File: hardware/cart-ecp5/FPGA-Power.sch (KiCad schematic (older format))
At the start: 2 parts

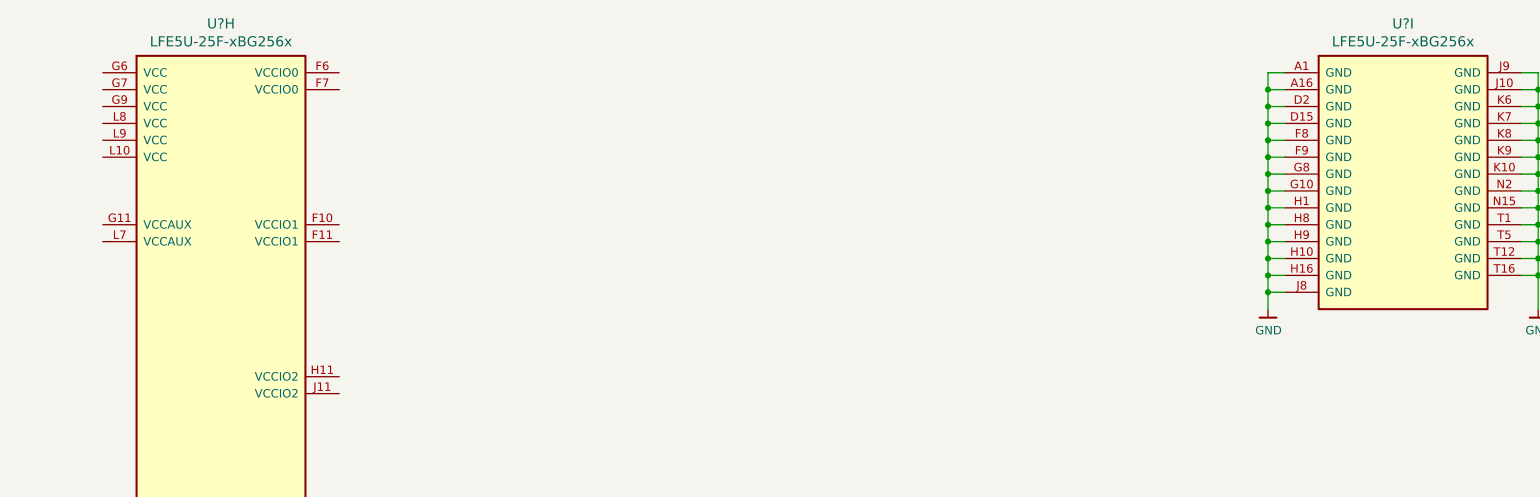
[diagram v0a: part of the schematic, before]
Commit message: First pass annotation and footprint assignment complete
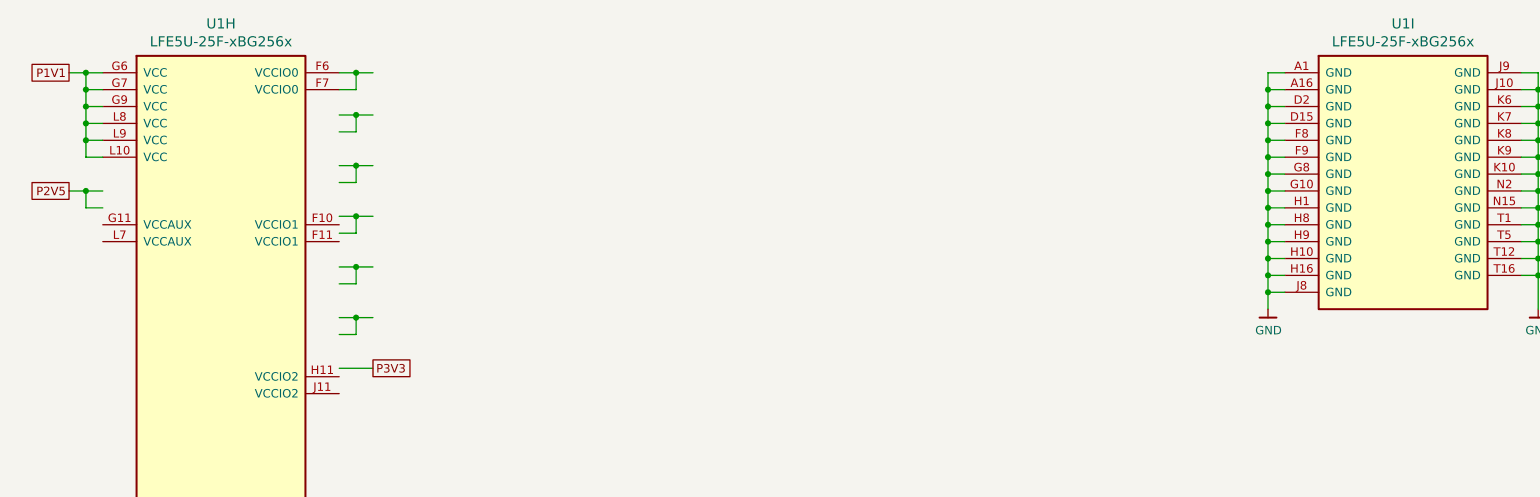
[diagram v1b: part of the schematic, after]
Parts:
- gave numbers to parts that had none: 1
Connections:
- net labels added: P1V1, P2V5, P3V3
- wire segments 54 -> 95
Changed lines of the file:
@@
 $EndDescr
 $Comp
-L ng_fpga_lattice_ecp5:LFE5U-25F-xBG256x U?
+L ng_fpga_lattice_ecp5:LFE5U-25F-xBG256x U1
 U 8 1 5F5F3F21
 P 5000 5000
-F 0 "U?" H 5500 5190 60  0000 C CNN
+F 0 "U1" H 5500 5190 60  0000 C CNN
 F 1 "LFE5U-25F-xBG256x" H 5500 5084 60  0000 C CNN
 F 2 "ng_fpga_lattice_ecp5:LFE5U-25F_BGA-256_14.0x14.0mm_Layout16x16_P0.8mm_Pad0.35mm" H 5750 950 60  0001 C CNN
@@
 $EndComp
 $Comp
-L ng_fpga_lattice_ecp5:LFE5U-25F-xBG256x U?
+L ng_fpga_lattice_ecp5:LFE5U-25F-xBG256x U1
 U 9 1 5F5F3F28
 P 12000 5000
-F 0 "U?" H 12500 5190 60  0000 C CNN
+F 0 "U1" H 12500 5190 60  0000 C CNN
 F 1 "LFE5U-25F-xBG256x" H 12500 5084 60  0000 C CNN
 F 2 "ng_fpga_lattice_ecp5:LFE5U-25F_BGA-256_14.0x14.0mm_Layout16x16_P0.8mm_Pad0.35mm" H 12750 950 60  0001 C CNN
@@
 	11700 6400 11700 6500
 $Comp
-L ng_power:GND #PWR?
+L ng_power:GND #PWR01
 U 1 1 5F5F3F7D
 P 11700 6500
-F 0 "#PWR?" H 11700 6250 50  0001 C CNN
+F 0 "#PWR01" H 11700 6250 50  0001 C CNN
 F 1 "GND" H 11703 6374 50  0000 C CNN
 F 2 "" H 11600 6150 50  0001 C CNN
@@
 $EndComp
 $Comp
-L ng_power:GND #PWR?
+L ng_power:GND #PWR02
 U 1 1 5F5F3F83
 P 13300 6500
-F 0 "#PWR?" H 13300 6250 50  0001 C CNN
+F 0 "#PWR02" H 13300 6250 50  0001 C CNN
 F 1 "GND" H 13303 6374 50  0000 C CNN
 F 2 "" H 13200 6150 50  0001 C CNN
@@
 	1    0    0    -1
 $EndComp
+Wire Wire Line
+	4800 5900 4700 5900
+Wire Wire Line
+	4700 5900 4700 5800
+Wire Wire Line
+	4700 5800 4800 5800
+Wire Wire Line
+	4700 5800 4600 5800
+Connection ~ 4700 5800
+Wire Wire Line
+	4800 5600 4700 5600
+Wire Wire Line
+	4700 5600 4700 5500
+Wire Wire Line
+	4700 5100 4800 5100
+Wire Wire Line
+	4800 5500 4700 5500
+Connection ~ 4700 5500
+Wire Wire Line
+	4700 5500 4700 5400
+Wire Wire Line
+	4700 5400 4800 5400
+Connection ~ 4700 5400
+Wire Wire Line
+	4700 5400 4700 5300
+Wire Wire Line
+	4800 5300 4700 5300
+Connection ~ 4700 5300
+Wire Wire Line
+	4700 5300 4700 5200
+Wire Wire Line
+	4700 5200 4800 5200
+Connection ~ 4700 5200
+Wire Wire Line
+	4700 5200 4700 5100
+Wire Wire Line
+	4700 5100 4600 5100
+Connection ~ 4700 5100
+Text GLabel 4600 5100 0    50   UnSpc ~ 0
+P1V1
+Text GLabel 4600 5800 0    50   UnSpc ~ 0
+P2V5
+Wire Wire Line
+	6200 6850 6400 6850
+Wire Wire Line
+	6200 6650 6300 6650
+Wire Wire Line
+	6300 6650 6300 6550
+Wire Wire Line
+	6300 6550 6200 6550
+Wire Wire Line
+	6200 6250 6300 6250
+Wire Wire Line
+	6300 6250 6300 6350
+Wire Wire Line
+	6300 6350 6200 6350
+Wire Wire Line
+	6200 5950 6300 5950
+Wire Wire Line
+	6300 5950 6300 6050
+Wire Wire Line
+	6300 6050 6200 6050
+Wire Wire Line
+	6200 5650 6300 5650
+Wire Wire Line
+	6200 5750 6300 5750
+Wire Wire Line
+	6300 5750 6300 5650
+Wire Wire Line
+	6200 5350 6300 5350
+Wire Wire Line
+	6300 5350 6300 5450
+Wire Wire Line
+	6300 5450 6200 5450
+Wire Wire Line
+	6200 5100 6300 5100
+Wire Wire Line
+	6300 5100 6300 5200
+Wire Wire Line
+	6300 5200 6200 5200
+Wire Wire Line
+	6300 5100 6400 5100
+Connection ~ 6300 5100
+Wire Wire Line
+	6300 5350 6400 5350
+Connection ~ 6300 5350
+Wire Wire Line
+	6300 5650 6400 5650
+Connection ~ 6300 5650
+Wire Wire Line
+	6300 5950 6400 5950
+Connection ~ 6300 5950
+Wire Wire Line
+	6300 6250 6400 6250
+Connection ~ 6300 6250
+Wire Wire Line
+	6300 6550 6400 6550
+Connection ~ 6300 6550
+Text GLabel 6400 6850 2    50   UnSpc ~ 0
+P3V3
 $EndSCHEMATC

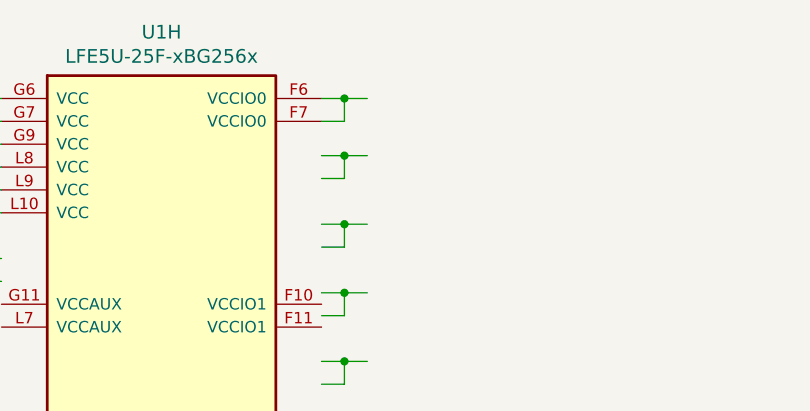
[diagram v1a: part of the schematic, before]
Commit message: Assign FPGA pins for N64 cartridge bus
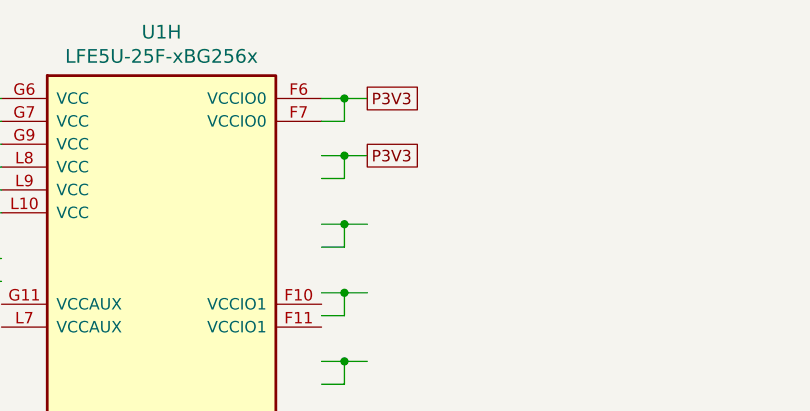
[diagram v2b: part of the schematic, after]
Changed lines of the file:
@@
 Text GLabel 6400 6850 2    50   UnSpc ~ 0
 P3V3
+Text GLabel 6400 5100 2    50   UnSpc ~ 0
+P3V3
+Text GLabel 6400 5350 2    50   UnSpc ~ 0
+P3V3
 $EndSCHEMATC

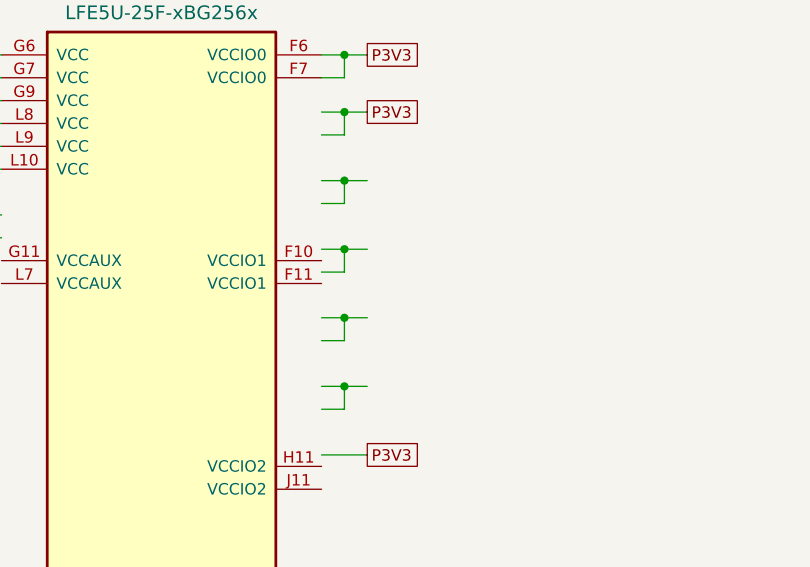
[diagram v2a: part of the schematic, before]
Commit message: Refine placement to make room for power management
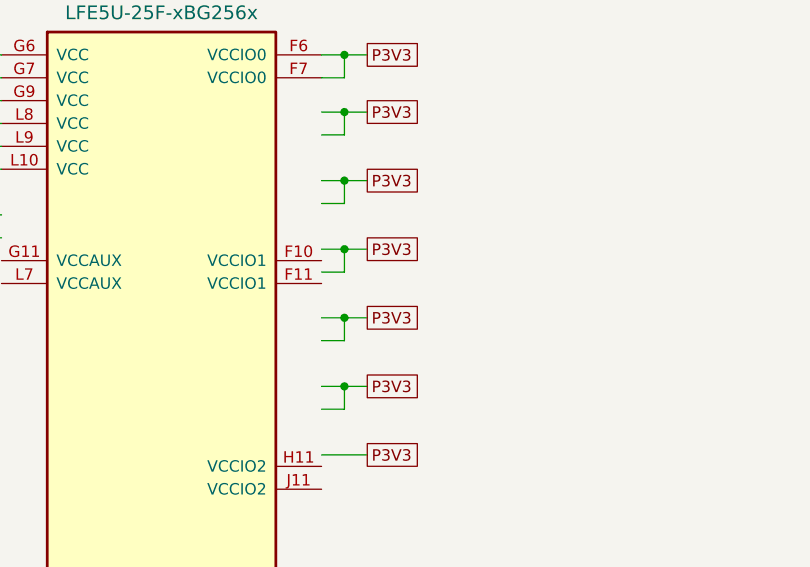
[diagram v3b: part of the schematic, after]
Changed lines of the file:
@@
 Text GLabel 6400 5350 2    50   UnSpc ~ 0
 P3V3
+Text GLabel 6400 5650 2    50   UnSpc ~ 0
+P3V3
+Text GLabel 6400 5950 2    50   UnSpc ~ 0
+P3V3
+Text GLabel 6400 6250 2    50   UnSpc ~ 0
+P3V3
+Text GLabel 6400 6550 2    50   UnSpc ~ 0
+P3V3
 $EndSCHEMATC

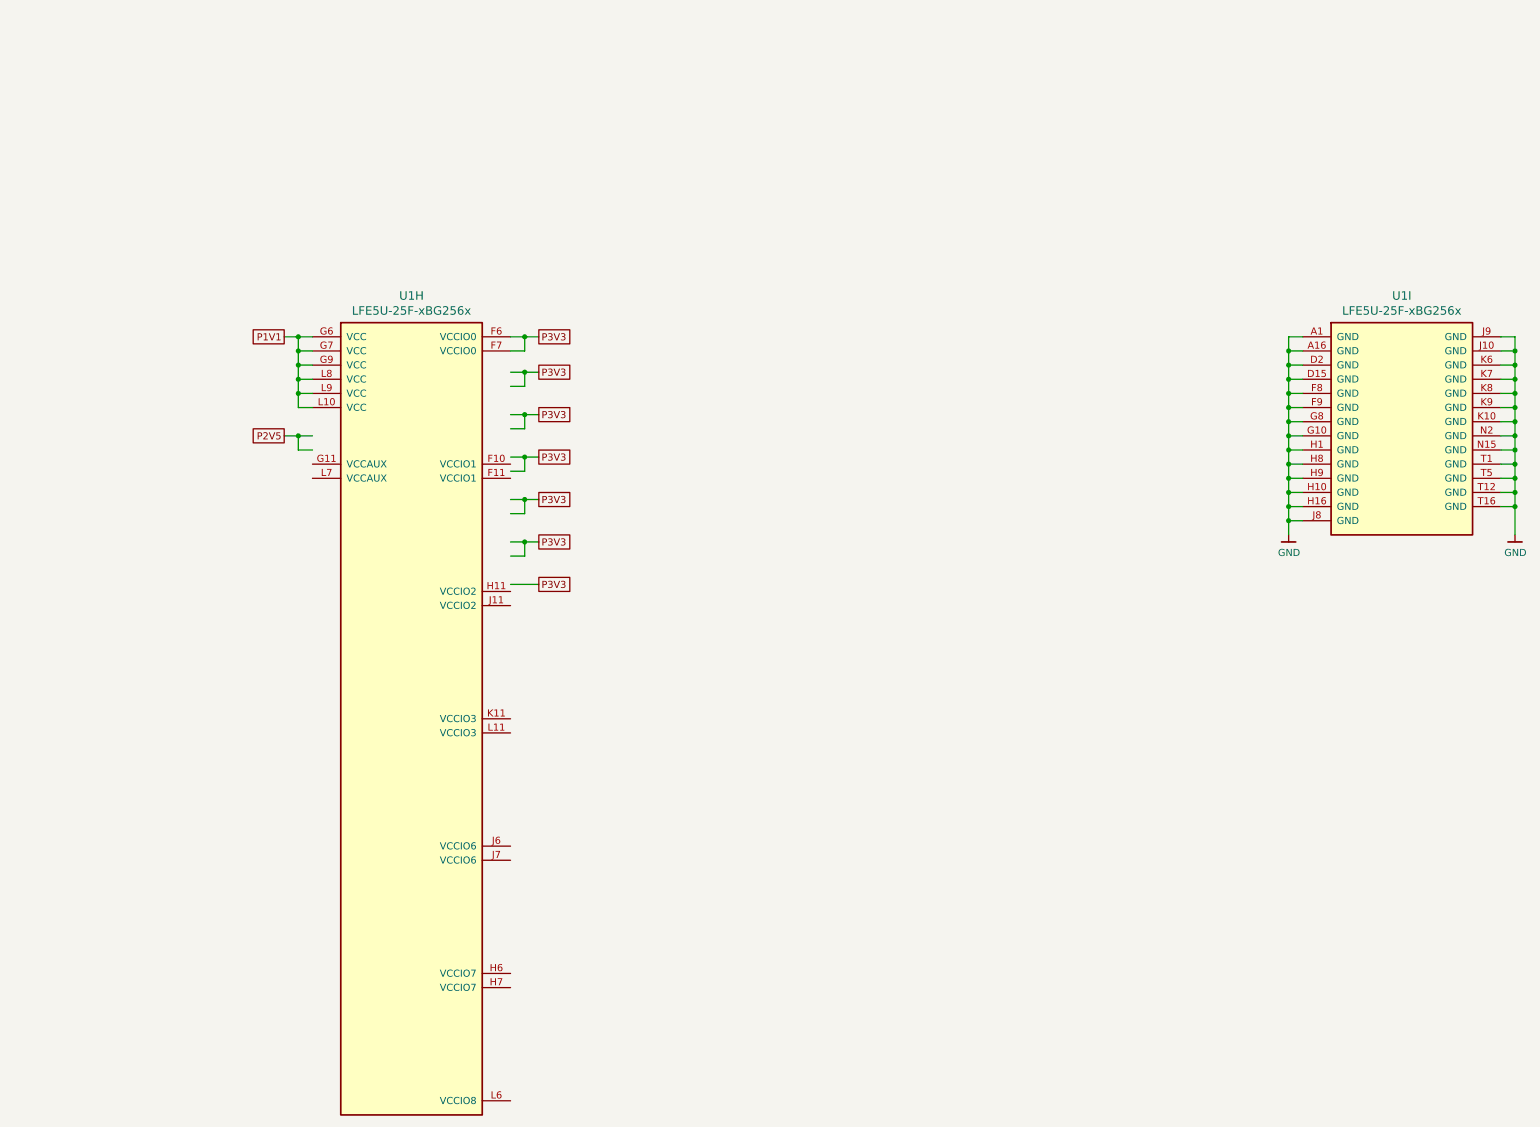
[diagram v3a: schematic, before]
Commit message: Add FPGA decoupling to schematic
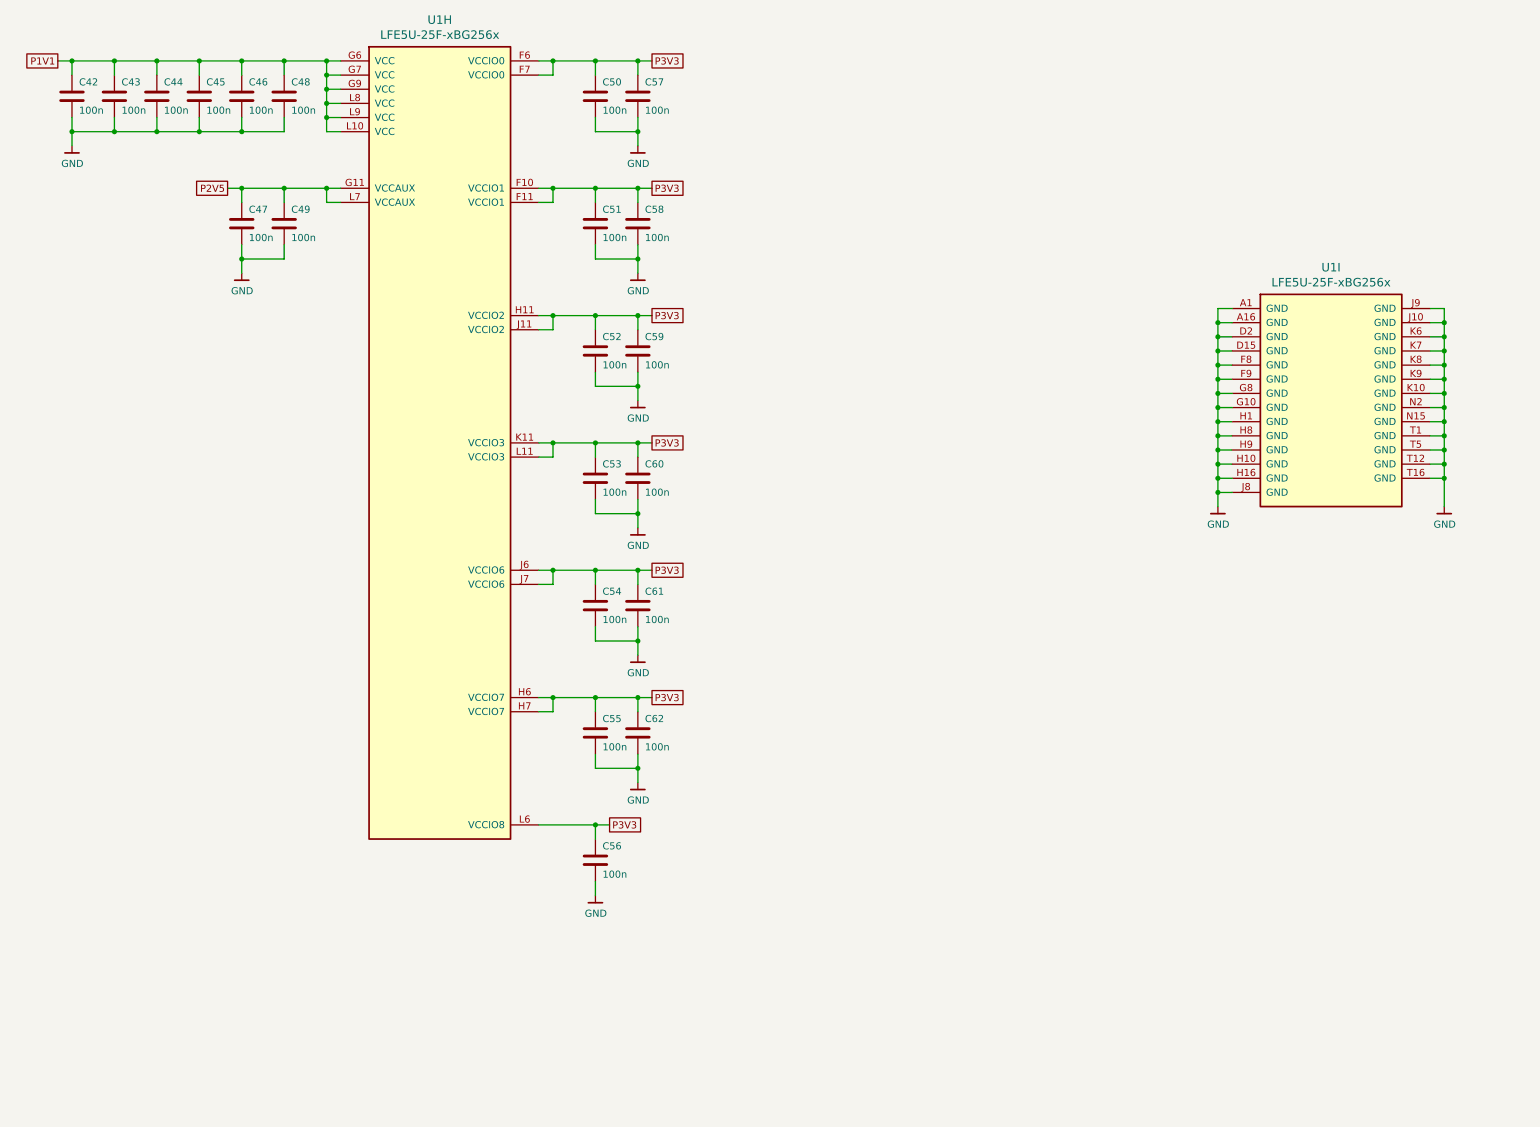
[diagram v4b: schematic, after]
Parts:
- added C42, C43, C44, C45, C46, C47, C48, C49, C50, C51, C52, C53, C54, C55, C56, C57, C58, C59, C60, C61, C62: 100n, Capacitor_SMD:C_0402_1005Metric, symbol Device:C
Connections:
- wire segments 95 -> 178
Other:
- moved on the sheet: U1H, U1I

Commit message: Use 1V8 for HyperRAM interface
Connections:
- net P3V3: no longer C55.1, C62.1, U1.H6 (VCCIO7), U1.H7 (VCCIO7)
- new net P1V8: C55.1, C62.1, U1.H6 (VCCIO7), U1.H7 (VCCIO7)
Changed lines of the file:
@@
 Connection ~ 6500 7650
 Text GLabel 7200 7650 2    50   UnSpc ~ 0
-P3V3
+P1V8
 $Comp
 L Device:C C62

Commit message: Move low-value FPGA decoupling caps to bottom layer
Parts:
- removed C48, C56, C60: 100n, Capacitor_SMD:C_0402_1005Metric, symbol Device:C
- C43, C46, C53, C54, C57, C62: value 100n -> 10n
- C45: value 100n -> 1u
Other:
- moved on the sheet: C42, C43, C44, C45, C46, C50, C51, C52, C53, C54, C57, C58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

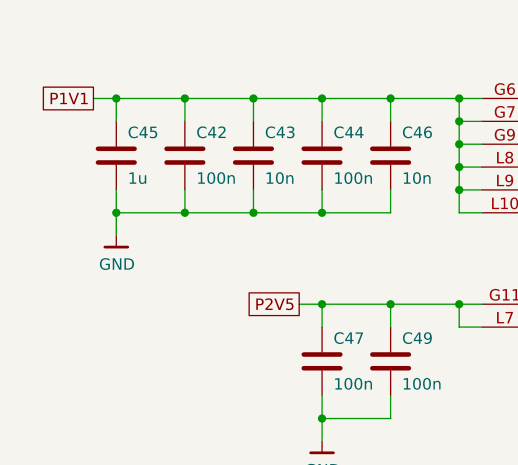
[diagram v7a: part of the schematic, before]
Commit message: Assign FPGA IO for main clock, adjust placement of core switcher
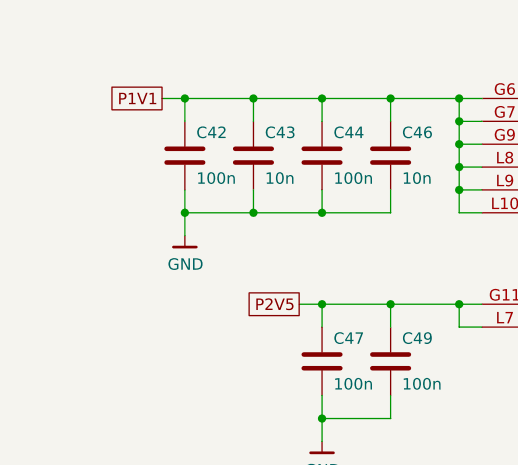
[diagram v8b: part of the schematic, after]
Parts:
- removed C45: 1u, Capacitor_SMD:C_0402_1005Metric, symbol Device:C
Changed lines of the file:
@@
 	4900 3150 4600 3150
 Connection ~ 4900 3150
-Text GLabel 3300 3150 0    50   UnSpc ~ 0
+Text GLabel 3600 3150 0    50   UnSpc ~ 0
 P1V1
 Text GLabel 4200 4050 0    50   UnSpc ~ 0
@@
 L ng_power:GND #PWR01
 U 1 1 5F9193F8
-P 3400 3750
-F 0 "#PWR01" H 3400 3500 50  0001 C CNN
-F 1 "GND" H 3403 3624 50  0000 C CNN
-F 2 "" H 3300 3400 50  0001 C CNN
-F 3 "" H 3400 3750 50  0001 C CNN
-	1    3400 3750
+P 3700 3750
+F 0 "#PWR01" H 3700 3500 50  0001 C CNN
+F 1 "GND" H 3703 3624 50  0000 C CNN
+F 2 "" H 3600 3400 50  0001 C CNN
+F 3 "" H 3700 3750 50  0001 C CNN
+	1    3700 3750
 	1    0    0    -1
 $EndComp
@@
 Wire Wire Line
 	4300 3150 4600 3150
-$Comp
-L Device:C C45
-U 1 1 5F933EBA
-P 3400 3400
-F 0 "C45" H 3450 3500 50  0000 L CNN
-F 1 "1u" H 3450 3300 50  0000 L CNN
-F 2 "Capacitor_SMD:C_0402_1005Metric" H 3438 3250 50  0001 C CNN
-F 3 "~" H 3400 3400 50  0001 C CNN
-	1    3400 3400
-	1    0    0    -1
-$EndComp
 Wire Wire Line
 	4000 3650 4000 3550
@@
 	1    0    0    -1
 $EndComp
-Wire Wire Line
-	3400 3650 3400 3550
-Wire Wire Line
-	3400 3250 3400 3150
 $Comp
 L Device:C C42
@@
 	1    0    0    -1
 $EndComp
-Connection ~ 3400 3150
-Wire Wire Line
-	3400 3150 3700 3150
 Connection ~ 3700 3150
 Wire Wire Line
 	3700 3150 4000 3150
-Wire Wire Line
-	3400 3650 3700 3650
-Connection ~ 3700 3650
 Wire Wire Line
 	3700 3650 4000 3650
@@
 	4300 3650 4600 3650
 Wire Wire Line
-	3400 3650 3400 3750
+	3700 3650 3700 3750
 $Comp
 L Device:C C49
@@
 	1    0    0    -1
 $EndComp
-Connection ~ 3400 3650
-Wire Wire Line
-	3300 3150 3400 3150
+Connection ~ 3700 3650
+Wire Wire Line
+	3600 3150 3700 3150
 $EndSCHEMATC
